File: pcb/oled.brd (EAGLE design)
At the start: 26.2 x 26.2 mm, 21 parts, among them U1 UG-2828GDEDF11, U2 FAN5331SX

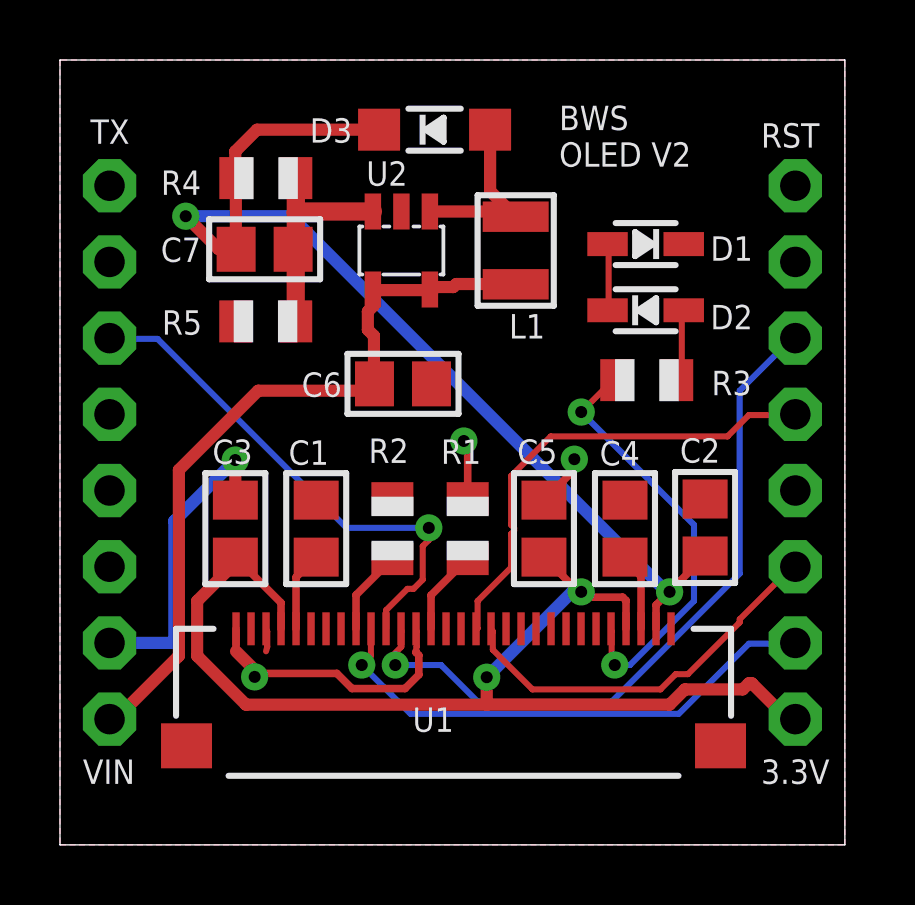
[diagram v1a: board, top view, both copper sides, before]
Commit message: Use GPIO2 instead of GPIO5(SCL) for OLED DC pin
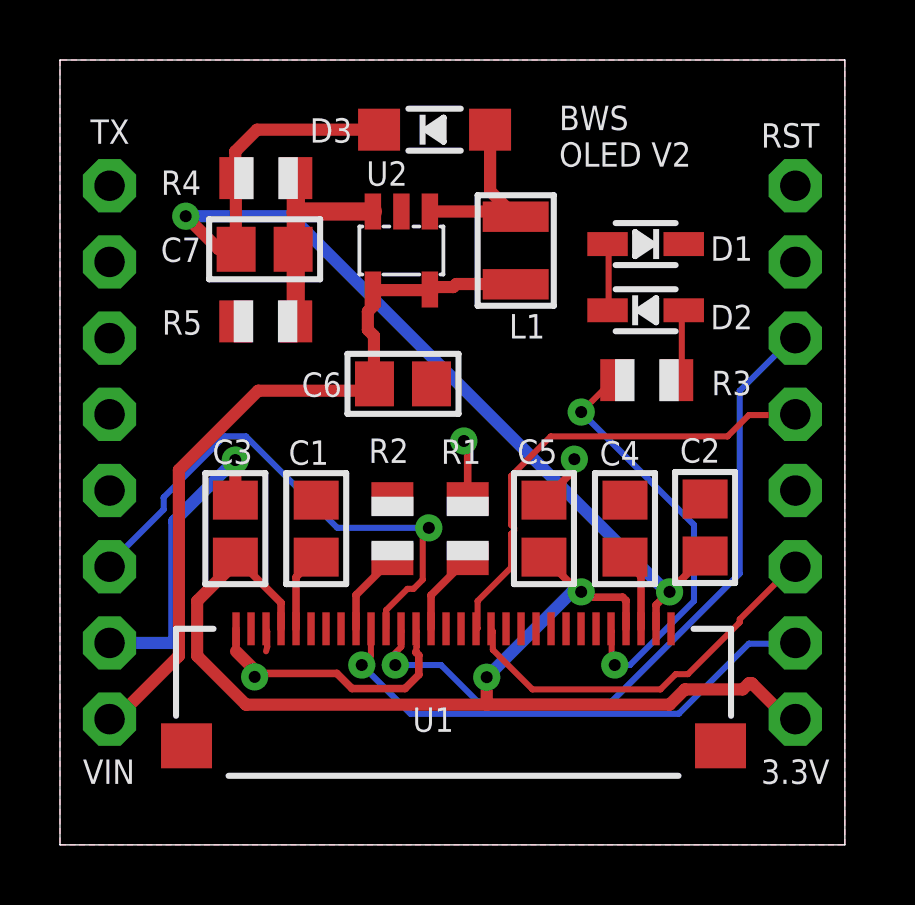
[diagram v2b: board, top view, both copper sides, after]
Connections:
- net D1/GPIO5: no longer U1.P$11
- net D4/GPIO2: now also U1.P$11
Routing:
- net D4/GPIO2: track 0.00 -> 18.1 mm, vias 0 -> 1
- net D1/GPIO5: track 17.3 -> 0.08 mm, vias 1 -> 0
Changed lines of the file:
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@@
 <grid distance="0.005" unitdist="inch" unit="inch" style="lines" multiple="1" display="no" altdistance="0.025" altunitdist="inch" altunit="inch"/>
 <layers>
-<layer number="1" name="Top" color="4" fill="1" visible="no" active="yes"/>
+<layer number="1" name="Top" color="4" fill="1" visible="yes" active="yes"/>
 <layer number="2" name="Route2" color="1" fill="3" visible="no" active="no"/>
 <layer number="3" name="Route3" color="4" fill="3" visible="no" active="no"/>
@@
 <signal name="D1/GPIO5">
 <contactref element="JP1" pad="3"/>
+<wire x1="1.7272" y1="16.8656" x2="1.651" y2="16.891" width="0.2032" layer="16"/>
+</signal>
+<signal name="D2/GPIO4">
+<contactref element="JP1" pad="4"/>
+</signal>
+<signal name="D3/GPIO0">
+<contactref element="JP1" pad="5"/>
+</signal>
+<signal name="D4/GPIO2">
+<contactref element="JP1" pad="6"/>
 <contactref element="U1" pad="P$11"/>
 <wire x1="10.8712" y1="7.8232" x2="10.8712" y2="7.2136" width="0.2032" layer="1"/>
@@
 <wire x1="11.7856" y1="8.5344" x2="11.5824" y2="8.5344" width="0.2032" layer="1"/>
 <wire x1="12.0904" y1="8.8392" x2="11.7856" y2="8.5344" width="0.2032" layer="1"/>
-<wire x1="12.0904" y1="9.9568" x2="12.0904" y2="8.8392" width="0.2032" layer="1"/>
-<wire x1="12.2936" y1="10.16" x2="12.0904" y2="9.9568" width="0.2032" layer="1"/>
-<wire x1="12.2936" y1="10.5664" x2="12.2936" y2="10.16" width="0.2032" layer="1"/>
-<wire x1="9.5504" y1="10.5664" x2="12.2936" y2="10.5664" width="0.2032" layer="16"/>
-<wire x1="3.2512" y1="16.8656" x2="9.5504" y2="10.5664" width="0.2032" layer="16"/>
-<wire x1="1.7272" y1="16.8656" x2="3.2512" y2="16.8656" width="0.2032" layer="16"/>
+<wire x1="12.0904" y1="10.3632" x2="12.0904" y2="8.8392" width="0.2032" layer="1"/>
+<wire x1="12.2936" y1="10.5664" x2="12.0904" y2="10.3632" width="0.2032" layer="1"/>
+<wire x1="9.2456" y1="10.5664" x2="12.2936" y2="10.5664" width="0.2032" layer="16"/>
+<wire x1="6.1976" y1="13.6144" x2="9.2456" y2="10.5664" width="0.2032" layer="16"/>
+<wire x1="5.4864" y1="13.6144" x2="6.1976" y2="13.6144" width="0.2032" layer="16"/>
+<wire x1="3.4544" y1="11.5824" x2="5.4864" y2="13.6144" width="0.2032" layer="16"/>
+<wire x1="3.4544" y1="11.176" x2="3.4544" y2="11.5824" width="0.2032" layer="16"/>
+<wire x1="1.6256" y1="9.3472" x2="3.4544" y2="11.176" width="0.2032" layer="16"/>
 <wire x1="10.8712" y1="7.2136" x2="10.868" y2="7.202" width="0.2032" layer="1"/>
-<wire x1="1.7272" y1="16.8656" x2="1.651" y2="16.891" width="0.2032" layer="16"/>
+<wire x1="1.6256" y1="9.3472" x2="1.651" y2="9.271" width="0.2032" layer="16"/>
 <via x="12.2936" y="10.5664" extent="1-16" drill="0.4"/>
 </signal>
-<signal name="D2/GPIO4">
-<contactref element="JP1" pad="4"/>
-</signal>
-<signal name="D3/GPIO0">
-<contactref element="JP1" pad="5"/>
-</signal>
-<signal name="D4/GPIO2">
-<contactref element="JP1" pad="6"/>
-</signal>
 <signal name="D8/GPIO15">

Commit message: Oled board v3 ordered
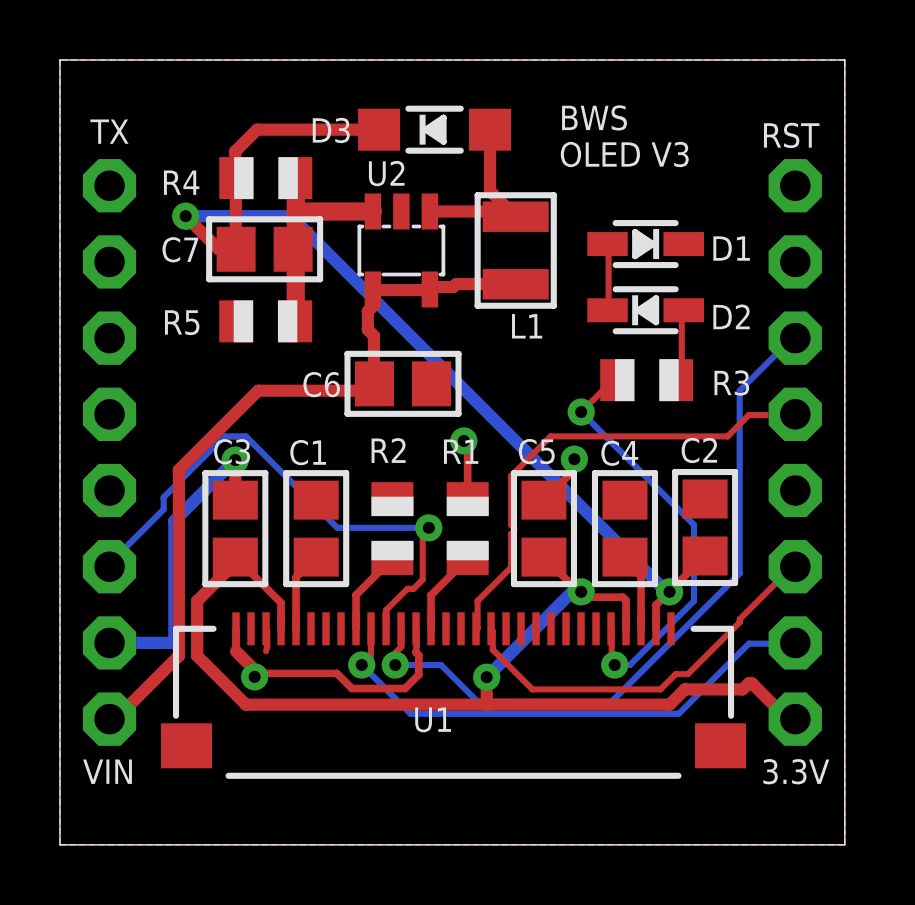
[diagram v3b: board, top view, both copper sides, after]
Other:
- board text added: "BWS OLED V3"
- board text removed: "BWS OLED V2"
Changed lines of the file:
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@@
 <layer number="14" name="Route14" color="1" fill="6" visible="no" active="no"/>
 <layer number="15" name="Route15" color="4" fill="6" visible="no" active="no"/>
-<layer number="16" name="Bottom" color="1" fill="1" visible="yes" active="yes"/>
+<layer number="16" name="Bottom" color="1" fill="1" visible="no" active="yes"/>
 <layer number="17" name="Pads" color="2" fill="1" visible="yes" active="yes"/>
 <layer number="18" name="Vias" color="2" fill="1" visible="yes" active="yes"/>
 <layer number="19" name="Unrouted" color="6" fill="1" visible="yes" active="yes"/>
 <layer number="20" name="Dimension" color="15" fill="1" visible="yes" active="yes"/>
-<layer number="21" name="tPlace" color="14" fill="1" visible="no" active="yes"/>
-<layer number="22" name="bPlace" color="5" fill="1" visible="yes" active="yes"/>
-<layer number="23" name="tOrigins" color="14" fill="1" visible="no" active="yes"/>
-<layer number="24" name="bOrigins" color="13" fill="1" visible="yes" active="yes"/>
-<layer number="25" name="tNames" color="7" fill="1" visible="no" active="yes"/>
-<layer number="26" name="bNames" color="7" fill="1" visible="yes" active="yes"/>
+<layer number="21" name="tPlace" color="14" fill="1" visible="yes" active="yes"/>
+<layer number="22" name="bPlace" color="5" fill="1" visible="no" active="yes"/>
+<layer number="23" name="tOrigins" color="14" fill="1" visible="yes" active="yes"/>
+<layer number="24" name="bOrigins" color="13" fill="1" visible="no" active="yes"/>
+<layer number="25" name="tNames" color="7" fill="1" visible="yes" active="yes"/>
+<layer number="26" name="bNames" color="7" fill="1" visible="no" active="yes"/>
 <layer number="27" name="tValues" color="7" fill="1" visible="no" active="yes"/>
 <layer number="28" name="bValues" color="7" fill="1" visible="no" active="yes"/>
@@
 <layer number="37" name="tTest" color="7" fill="1" visible="no" active="yes"/>
 <layer number="38" name="bTest" color="7" fill="1" visible="no" active="yes"/>
-<layer number="39" name="tKeepout" color="4" fill="11" visible="no" active="yes"/>
-<layer number="40" name="bKeepout" color="1" fill="11" visible="yes" active="yes"/>
-<layer number="41" name="tRestrict" color="4" fill="10" visible="no" active="yes"/>
-<layer number="42" name="bRestrict" color="1" fill="10" visible="yes" active="yes"/>
+<layer number="39" name="tKeepout" color="4" fill="11" visible="yes" active="yes"/>
+<layer number="40" name="bKeepout" color="1" fill="11" visible="no" active="yes"/>
+<layer number="41" name="tRestrict" color="4" fill="10" visible="yes" active="yes"/>
+<layer number="42" name="bRestrict" color="1" fill="10" visible="no" active="yes"/>
 <layer number="43" name="vRestrict" color="2" fill="10" visible="no" active="yes"/>
 <layer number="44" name="Drills" color="7" fill="1" visible="no" active="yes"/>
@@
 <layer number="49" name="Reference" color="7" fill="1" visible="no" active="yes"/>
 <layer number="50" name="dxf" color="7" fill="1" visible="no" active="yes"/>
-<layer number="51" name="tDocu" color="7" fill="1" visible="no" active="yes"/>
-<layer number="52" name="bDocu" color="7" fill="1" visible="yes" active="yes"/>
+<layer number="51" name="tDocu" color="7" fill="1" visible="yes" active="yes"/>
+<layer number="52" name="bDocu" color="7" fill="1" visible="no" active="yes"/>
 <layer number="53" name="tGND_GNDA" color="7" fill="9" visible="no" active="no"/>
 <layer number="54" name="bGND_GNDA" color="1" fill="9" visible="no" active="no"/>
@@
 <text x="2.794" y="4.572" size="0.8128" layer="26" rot="MR180" grouprefs="EVERYTHING">VIN</text>
 <text x="16.637" y="22.606" size="0.8128" layer="25" font="vector">BWS
-OLED V2</text>
+OLED V3</text>
 </plain>
 <attributes>
@@
 </element>
 <element name="JP2" library="adafruit" library_urn="urn:adsk.eagle:library:420" package="1X08-CLEANBIG" package3d_urn="urn:adsk.eagle:package:6240708/1" value="" x="24.511" y="13.081" smashed="yes" rot="R90" grouprefs="EVERYTHING">
+<attribute name="MPN" value="10129378-908001BLF" x="24.511" y="13.081" size="1.778" layer="27" rot="R90" display="off"/>
 <attribute name="POPULATE" value="0" x="24.511" y="13.081" size="1.778" layer="27" rot="R90" display="off"/>
 <attribute name="VALUE" x="27.686" y="2.921" size="1.27" layer="27" rot="R90"/>
 </element>
 <element name="JP1" library="adafruit" library_urn="urn:adsk.eagle:library:420" package="1X08-CLEANBIG" package3d_urn="urn:adsk.eagle:package:6240708/1" value="" x="1.651" y="13.081" smashed="yes" rot="R270" grouprefs="EVERYTHING">
+<attribute name="MPN" value="10129378-908001BLF" x="1.651" y="13.081" size="1.778" layer="27" rot="R270" display="off"/>
 <attribute name="POPULATE" value="0" x="1.651" y="13.081" size="1.778" layer="27" rot="R270" display="off"/>
 <attribute name="VALUE" x="-1.524" y="23.241" size="1.27" layer="27" rot="R270"/>
@@
 <signal name="D1/GPIO5">
 <contactref element="JP1" pad="3"/>
-<wire x1="1.7272" y1="16.8656" x2="1.651" y2="16.891" width="0.2032" layer="16"/>
 </signal>
 <signal name="D2/GPIO4">
